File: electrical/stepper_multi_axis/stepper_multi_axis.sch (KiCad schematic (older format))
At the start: 12 parts, among them J11 Conn_01x01_Male, J12 Conn_01x01_Male, J13 Conn_01x06, J14 Conn_01x01_Male, J15 Conn_01x01_Male, J16 Conn_01x01_Male, J17 Conn_01x01_Male, J18 Conn_01x01_Male

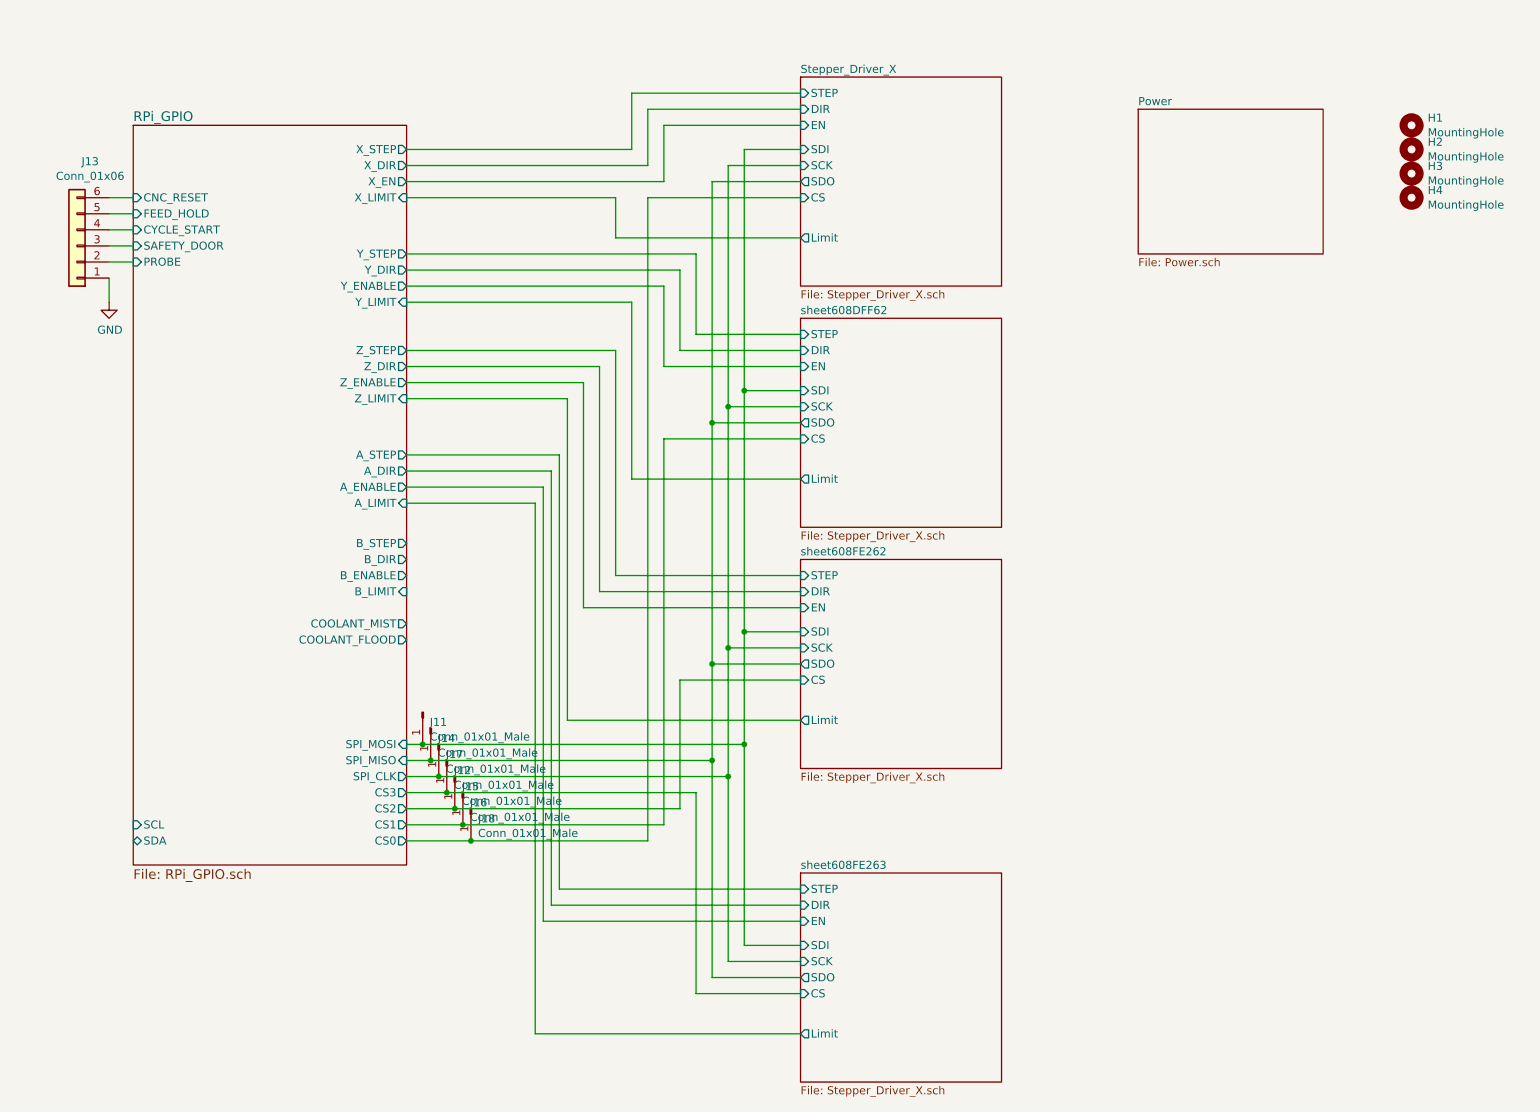
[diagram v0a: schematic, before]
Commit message: added higher current drivers
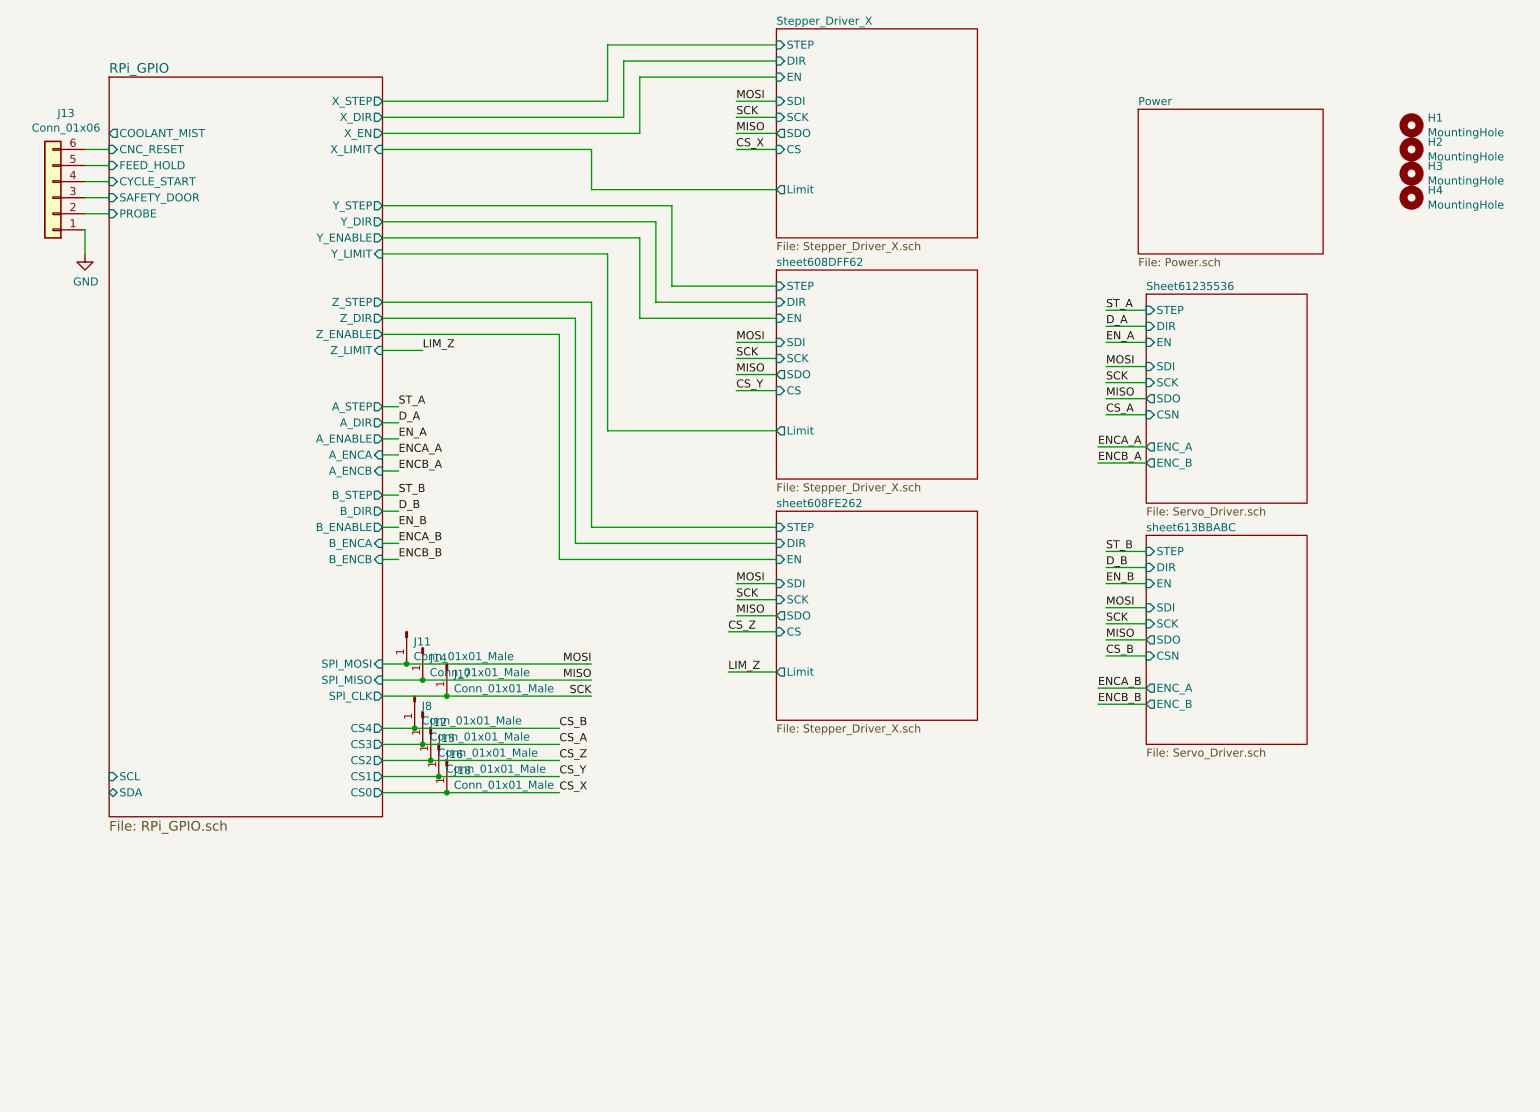
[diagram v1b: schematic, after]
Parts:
- added J8: Conn_01x01_Male, Connector_PinHeader_2.54mm:PinHeader_1x01_P2.54mm_Vertical, symbol Connector:Conn_01x01_Male
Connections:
- net RPi_GPIO/CS0 renamed CS_X
- net RPi_GPIO/CS1 renamed CS_Y
- net RPi_GPIO/CS2 renamed CS_Z
- net RPi_GPIO/CS3 renamed CS_A
- net RPi_GPIO/SPI_CLK renamed SCK
- net RPi_GPIO/SPI_MISO renamed MISO
- net RPi_GPIO/SPI_MOSI renamed MOSI
- new net CS_B: J8.1 (Pin_1)
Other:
- moved on the sheet: J11, J12, J13, J14, J15, J16, J17, J18

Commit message: shipped things
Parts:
- removed J13: Conn_01x06, Connector_PinSocket_2.54mm:PinSocket_1x06_P2.54mm_Vertical, symbol Connector_Generic:Conn_01x06
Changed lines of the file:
@@
 $Descr A4 11693 8268
 encoding utf-8
-Sheet 1 8
+Sheet 1 10
 Title ""
 Date ""
@@
 F1 "Power.sch" 50
 $EndSheet
-$Comp
-L Connector_Generic:Conn_01x06 J13
-U 1 1 60B4FC75
-P 1000 1600
-F 0 "J13" H 918 1075 50  0000 C CNN
-F 1 "Conn_01x06" H 918 1166 50  0000 C CNN
-F 2 "Connector_PinSocket_2.54mm:PinSocket_1x06_P2.54mm_Vertical" H 1000 1600 50  0001 C CNN
-F 3 "~" H 1000 1600 50  0001 C CNN
-	1    1000 1600
-	-1   0    0    1
-$EndComp
 $Sheet
 S 1350 850  1700 4600
@@
 F39 "B_ENCB" I R 3050 3850 50
 $EndSheet
-Wire Wire Line
-	1350 1300 1200 1300
-Wire Wire Line
-	1350 1400 1200 1400
-Wire Wire Line
-	1350 1500 1200 1500
-Wire Wire Line
-	1350 1600 1200 1600
-Wire Wire Line
-	1350 1700 1200 1700
-$Comp
-L power:GND #PWR0158
-U 1 1 60B600ED
-P 1200 1950
-F 0 "#PWR0158" H 1200 1700 50  0001 C CNN
-F 1 "GND" H 1205 1777 50  0000 C CNN
-F 2 "" H 1200 1950 50  0001 C CNN
-F 3 "" H 1200 1950 50  0001 C CNN
-	1    1200 1950
-	1    0    0    -1
-$EndComp
-Wire Wire Line
-	1200 1800 1200 1950
 $Comp
 L Mechanical:MountingHole H1
@@
 Text Label 5250 1300 0    50   ~ 0
 CS_X
+$Sheet
+S 1350 5750 950  800
+U 613FBD86
+F0 "Sheet613FBD85" 50
+F1 "CM4.sch" 50
+F2 "RX" I R 2300 5850 50
+F3 "TX" O R 2300 5950 50
+F4 "SWDIO" B R 2300 6050 50
+F5 "SWDCLK" O R 2300 6150 50
+F6 "USB_N" B R 2300 6250 50
+F7 "USB_P" B R 2300 6350 50
+F8 "USB_OTG" I R 2300 6450 50
+$EndSheet
+$Sheet
+S 2900 5750 950  800
+U 614CFDB7
+F0 "Sheet614CFDB6" 50
+F1 "USBHub.sch" 50
+F2 "USB_N" B L 2900 6250 50
+F3 "USP_P" B L 2900 6350 50
+F4 "USB_OTG" O L 2900 6450 50
+$EndSheet
+Wire Wire Line
+	2300 6250 2900 6250
+Wire Wire Line
+	2300 6350 2900 6350
+Wire Wire Line
+	2300 6450 2900 6450
 $EndSCHEMATC

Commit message: pre delete thru hole
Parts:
- removed H2, H3, H4: MountingHole, MountingHole:MountingHole_3.2mm_M3, symbol Mechanical:MountingHole
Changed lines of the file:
@@
 F38 "CS4" O R 3050 4900 50
 F39 "B_ENCB" I R 3050 3850 50
+F40 "USB_TEENSY_P" B L 1350 5000 50
+F41 "USB_TEENSY_N" B L 1350 4900 50
 $EndSheet
 $Comp
@@
 F 3 "~" H 9450 1150 50  0001 C CNN
 	1    9450 1150
-	1    0    0    -1
-$EndComp
-$Comp
-L Mechanical:MountingHole H2
-U 1 1 60F7D759
-P 9450 1300
-F 0 "H2" H 9550 1346 50  0000 L CNN
-F 1 "MountingHole" H 9550 1255 50  0000 L CNN
-F 2 "MountingHole:MountingHole_3.2mm_M3" H 9450 1300 50  0001 C CNN
-F 3 "~" H 9450 1300 50  0001 C CNN
-	1    9450 1300
-	1    0    0    -1
-$EndComp
-$Comp
-L Mechanical:MountingHole H3
-U 1 1 60F80BB5
-P 9450 1450
-F 0 "H3" H 9550 1496 50  0000 L CNN
-F 1 "MountingHole" H 9550 1405 50  0000 L CNN
-F 2 "MountingHole:MountingHole_3.2mm_M3" H 9450 1450 50  0001 C CNN
-F 3 "~" H 9450 1450 50  0001 C CNN
-	1    9450 1450
-	1    0    0    -1
-$EndComp
-$Comp
-L Mechanical:MountingHole H4
-U 1 1 60F84077
-P 9450 1600
-F 0 "H4" H 9550 1646 50  0000 L CNN
-F 1 "MountingHole" H 9550 1555 50  0000 L CNN
-F 2 "MountingHole:MountingHole_3.2mm_M3" H 9450 1600 50  0001 C CNN
-F 3 "~" H 9450 1600 50  0001 C CNN
-	1    9450 1600
 	1    0    0    -1
 $EndComp
@@
 CS_X
 $Sheet
-S 1350 5750 950  800
+S 750  6250 950  800
 U 613FBD86
 F0 "Sheet613FBD85" 50
 F1 "CM4.sch" 50
-F2 "RX" I R 2300 5850 50
-F3 "TX" O R 2300 5950 50
-F4 "SWDIO" B R 2300 6050 50
-F5 "SWDCLK" O R 2300 6150 50
-F6 "USB_N" B R 2300 6250 50
-F7 "USB_P" B R 2300 6350 50
-F8 "USB_OTG" I R 2300 6450 50
-$EndSheet
-$Sheet
-S 2900 5750 950  800
+F2 "RX" I R 1700 6350 50
+F3 "TX" O R 1700 6450 50
+F4 "SWDIO" B R 1700 6550 50
+F5 "SWDCLK" O R 1700 6650 50
+F6 "USB_N" B R 1700 6750 50
+F7 "USB_P" B R 1700 6850 50
+F8 "USB_OTG" I R 1700 6950 50
+$EndSheet
+$Sheet
+S 2300 6250 950  800
 U 614CFDB7
 F0 "Sheet614CFDB6" 50
 F1 "USBHub.sch" 50
-F2 "USB_N" B L 2900 6250 50
-F3 "USP_P" B L 2900 6350 50
-F4 "USB_OTG" O L 2900 6450 50
-$EndSheet
-Wire Wire Line
-	2300 6250 2900 6250
-Wire Wire Line
-	2300 6350 2900 6350
-Wire Wire Line
-	2300 6450 2900 6450
+F2 "USB_N" B L 2300 6750 50
+F3 "USP_P" B L 2300 6850 50
+F4 "USB_OTG" O L 2300 6950 50
+F5 "USB_INTERNAL_P" B L 2300 6500 50
+F6 "USB_INTERNAL_N" B L 2300 6600 50
+$EndSheet
+Wire Wire Line
+	1700 6750 2300 6750
+Wire Wire Line
+	1700 6850 2300 6850
+Wire Wire Line
+	1700 6950 2300 6950
+Wire Wire Line
+	2300 6500 2100 6500
+Wire Wire Line
+	2100 6500 2100 5600
+Wire Wire Line
+	2100 5600 1200 5600
+Wire Wire Line
+	1200 5600 1200 5000
+Wire Wire Line
+	1200 5000 1350 5000
+Wire Wire Line
+	1350 4900 1100 4900
+Wire Wire Line
+	1100 4900 1100 5700
+Wire Wire Line
+	1100 5700 2000 5700
+Wire Wire Line
+	2000 5700 2000 6600
+Wire Wire Line
+	2000 6600 2300 6600
 $EndSCHEMATC
